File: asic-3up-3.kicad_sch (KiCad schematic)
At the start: 81 parts, among them U24 MCP1824T-1202E/OT, U25 MCP1824T-1202E/OT, U26 MCP1824T-1202E/OT, U27 MCP1824T-0802E, U28 MCP1824T-0802E, U29 MCP1824T-0802E, U30 BM1362AC_MODE1, U31 BM1362AC_MODE0, U32 BM1362AC_MODE1

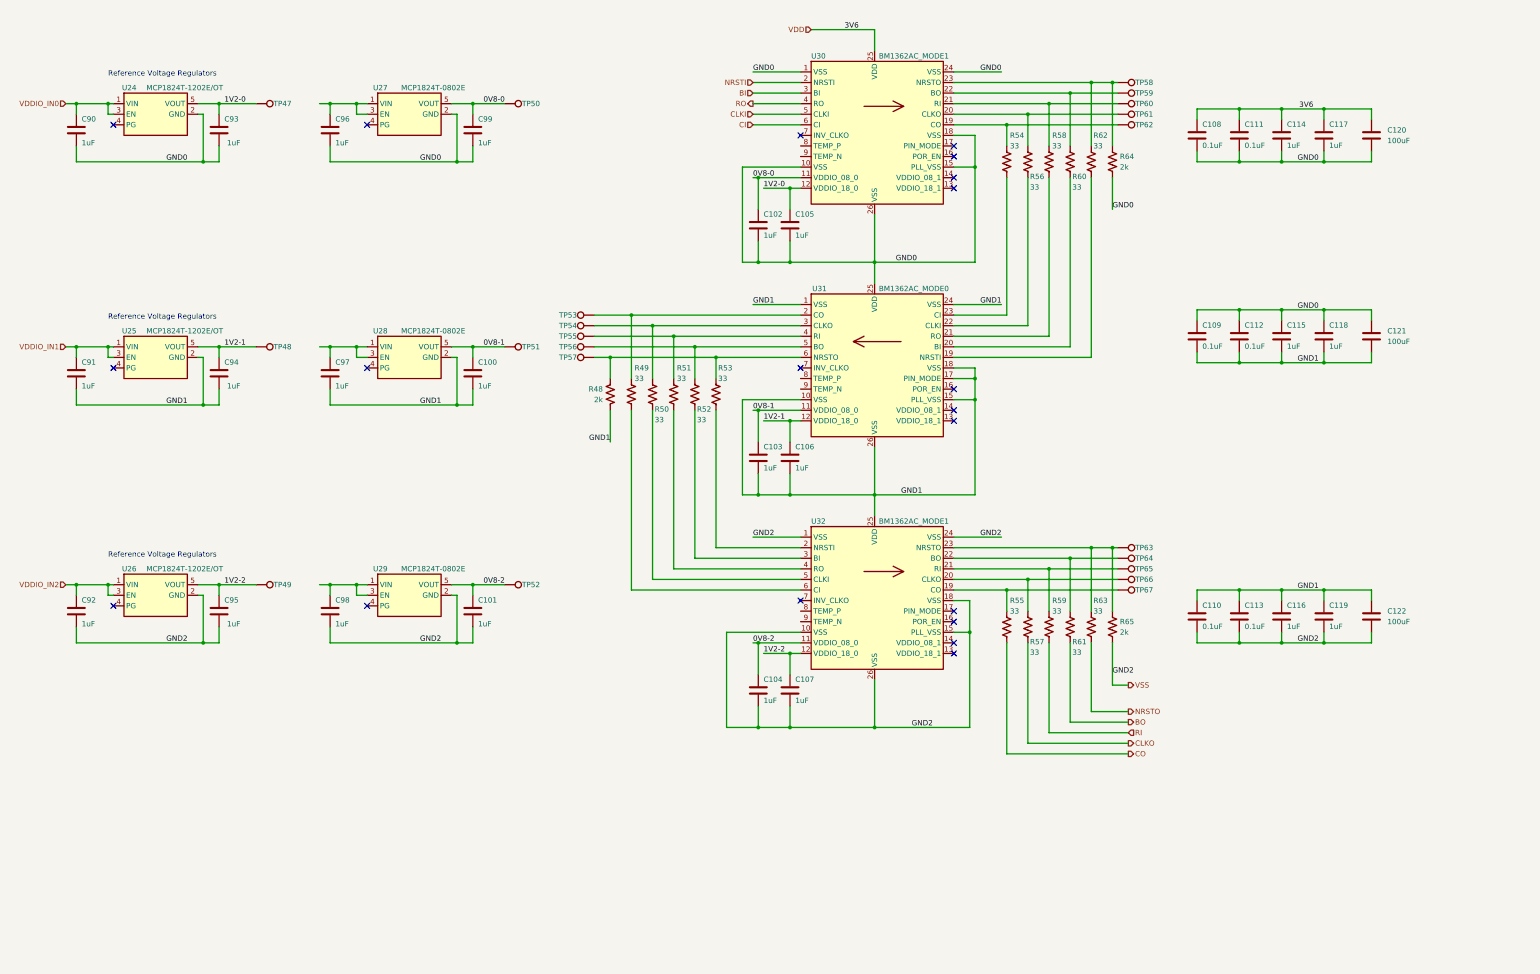
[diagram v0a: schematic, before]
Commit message: added all the ASICs to the schematic. added the RP2040 circuit for data. added the VDDIO boost circuit. schematic cleanup
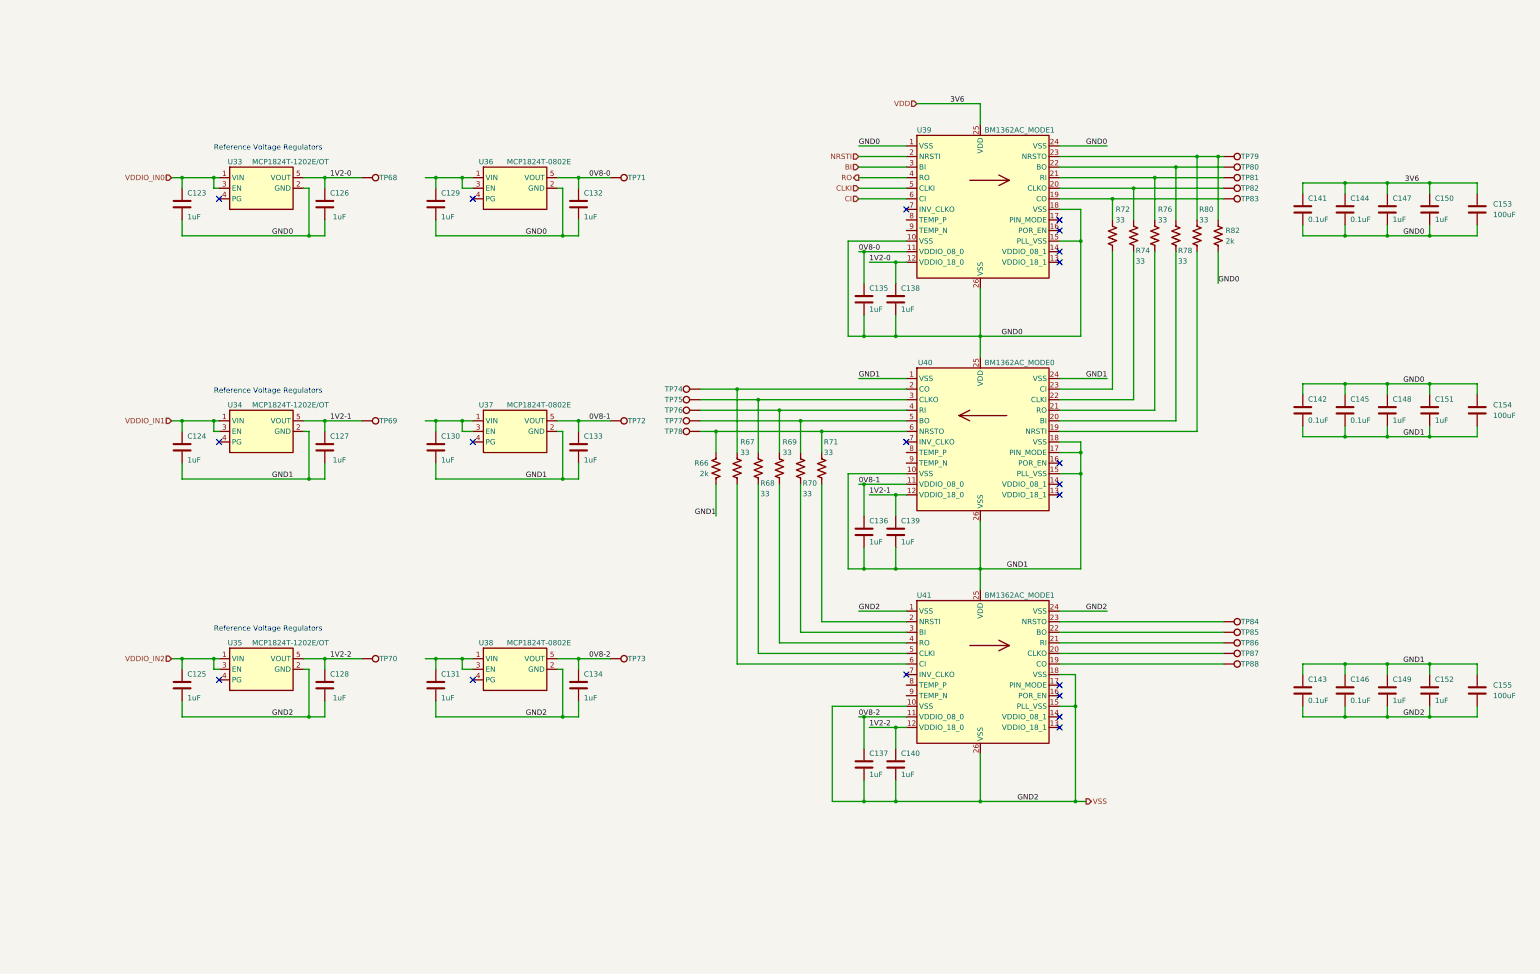
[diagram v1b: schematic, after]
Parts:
- removed R55, R57, R59, R61, R63: 33, Resistor_SMD:R_0402_1005Metric, symbol Device:R_US
- removed R65: 2k, Resistor_SMD:R_0402_1005Metric, symbol Device:R_US
- renumbered C90 to C123, C91 to C124, C92 to C125, C93 to C126, C94 to C127, C95 to C128, C96 to C129, C97 to C130, C98 to C131, C99 to C132, C100 to C133, C101 to C134, C102 to C135, C103 to C136, C104 to C137, C105 to C138, C106 to C139, C107 to C140, C108 to C141, C109 to C142, C110 to C143, C111 to C144, C112 to C145, C113 to C146, C114 to C147, C115 to C148, C116 to C149, C117 to C150, C118 to C151, C119 to C152, C120 to C153, C121 to C154, C122 to C155, R48 to R66, R49 to R67, R50 to R68, R51 to R69, R52 to R70, R53 to R71, R54 to R72, R56 to R74, R58 to R76, R60 to R78, R62 to R80, R64 to R82, TP47 to TP68, TP48 to TP69, TP49 to TP70, TP50 to TP71, TP51 to TP72, TP52 to TP73, TP53 to TP74, TP54 to TP75, TP55 to TP76, TP56 to TP77, TP57 to TP78, TP58 to TP79, TP59 to TP80, TP60 to TP81, TP61 to TP82, TP62 to TP83, TP63 to TP84, TP64 to TP85, TP65 to TP86, TP66 to TP87, TP67 to TP88, U24 to U33, U25 to U34, U26 to U35, U27 to U36, U28 to U37, U29 to U38, U30 to U39, U31 to U40, U32 to U41
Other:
- moved on the sheet: C123, C124, C125, C126, C127, C128, C129, C130, C131, C132, C133, C134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

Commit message: added sweet logo to schematic worksheet. Schematic cleanup.
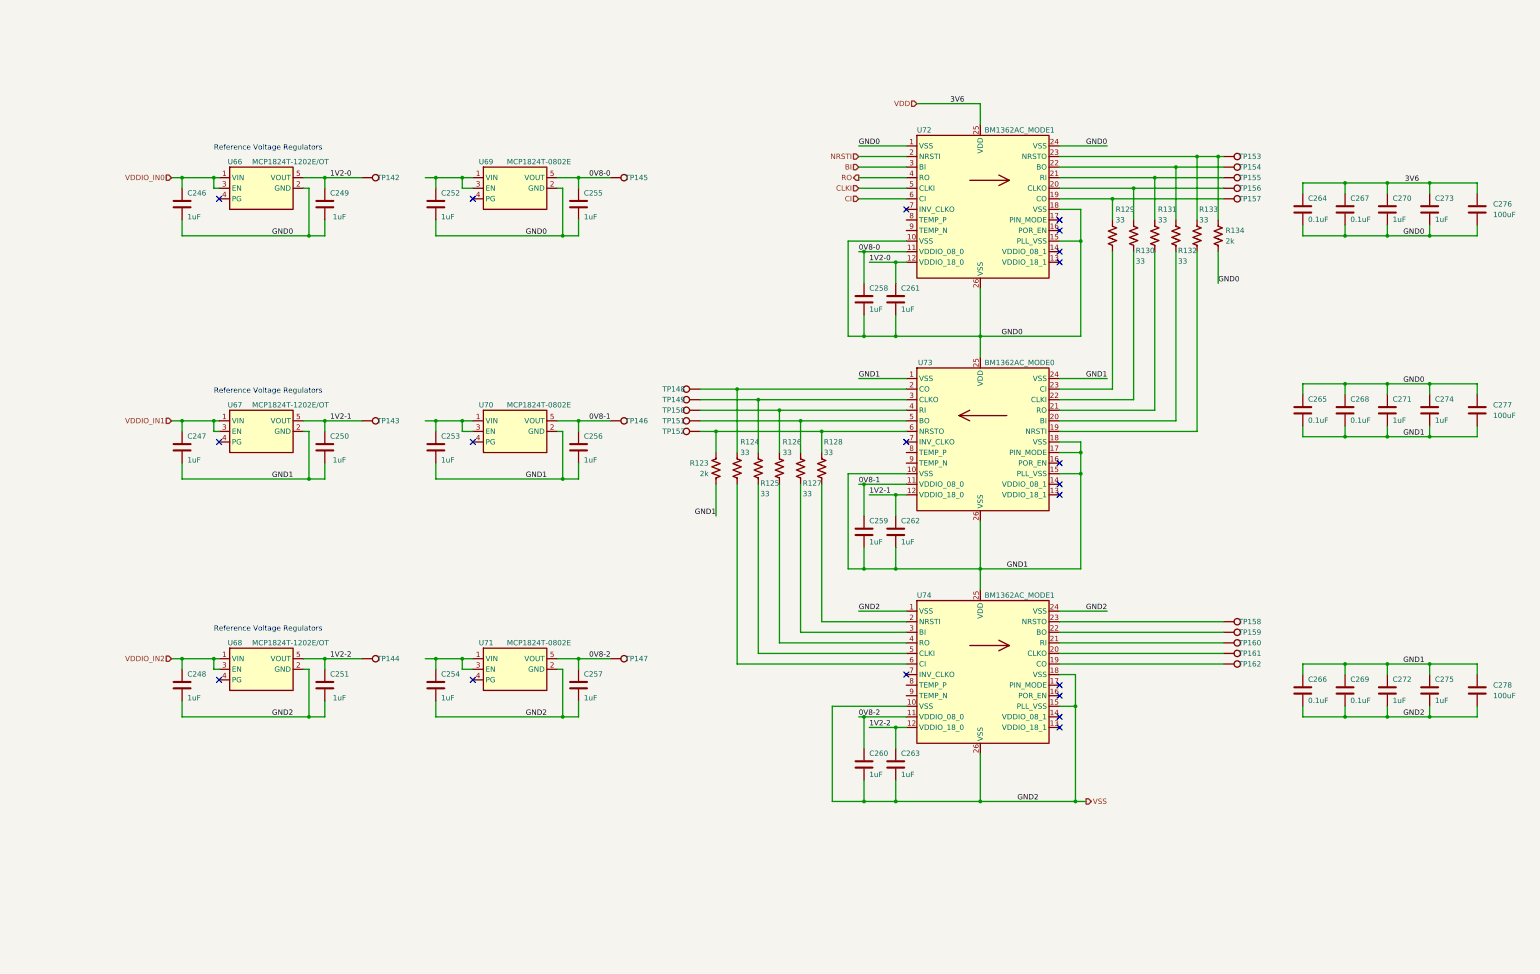
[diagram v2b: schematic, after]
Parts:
- renumbered C123 to C246, C124 to C247, C125 to C248, C126 to C249, C127 to C250, C128 to C251, C129 to C252, C130 to C253, C131 to C254, C132 to C255, C133 to C256, C134 to C257, C135 to C258, C136 to C259, C137 to C260, C138 to C261, C139 to C262, C140 to C263, C141 to C264, C142 to C265, C143 to C266, C144 to C267, C145 to C268, C146 to C269, C147 to C270, C148 to C271, C149 to C272, C150 to C273, C151 to C274, C152 to C275, C153 to C276, C154 to C277, C155 to C278, R66 to R123, R67 to R124, R68 to R125, R69 to R126, R70 to R127, R71 to R128, R72 to R129, R74 to R130, R76 to R131, R78 to R132, R80 to R133, R82 to R134, TP68 to TP142, TP69 to TP143, TP70 to TP144, TP71 to TP145, TP72 to TP146, TP73 to TP147, TP74 to TP148, TP75 to TP149, TP76 to TP150, TP77 to TP151, TP78 to TP152, TP79 to TP153, TP80 to TP154, TP81 to TP155, TP82 to TP156, TP83 to TP157, TP84 to TP158, TP85 to TP159, TP86 to TP160, TP87 to TP161, TP88 to TP162, U33 to U66, U34 to U67, U35 to U68, U36 to U69, U37 to U70, U38 to U71, U39 to U72, U40 to U73, U41 to U74

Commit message: starting layout
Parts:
- added J10, J11: Conn_01x01, emberone:5x9_powertab, symbol Connector_Generic:Conn_01x01
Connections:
- net GND0: now also J10.1 (Pin_1)
- net GND1: now also J11.1 (Pin_1)
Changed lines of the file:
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@@
 	)
 	(junction
+		(at 246.38 99.06)
+		(diameter 0)
+		(color 0 0 0 0)
+	)
+	(junction
 		(at 303.53 62.23)
 		(diameter 0)
@@
 	)
 	(junction
+		(at 246.38 156.21)
+		(diameter 0)
+		(color 0 0 0 0)
+	)
+	(junction
 		(at 226.06 105.41)
 		(diameter 0)
@@
 	(wire
 		(pts
+			(xy 246.38 99.06) (xy 246.38 105.41)
+		)
+		(stroke
+			(width 0)
+			(type default)
+		)
+	)
+	(wire
+		(pts
 			(xy 354.33 194.31) (xy 354.33 196.85)
 		)
@@
 	(wire
 		(pts
-			(xy 246.38 93.98) (xy 246.38 105.41)
+			(xy 246.38 93.98) (xy 246.38 99.06)
 		)
 		(stroke
@@
 	(wire
 		(pts
+			(xy 246.38 156.21) (xy 246.38 161.29)
+		)
+		(stroke
+			(width 0)
+			(type default)
+		)
+	)
+	(wire
+		(pts
 			(xy 334.01 78.74) (xy 334.01 81.28)
 		)
@@
 	(wire
 		(pts
-			(xy 246.38 149.86) (xy 246.38 161.29)
+			(xy 246.38 149.86) (xy 246.38 156.21)
 		)
 		(stroke
@@
 	)
 	(symbol
+		(lib_id "Connector_Generic:Conn_01x01")
+		(at 251.46 156.21 0)
+		(unit 1)
+		(exclude_from_sim no)
+		(in_bom yes)
+		(on_board yes)
+		(dnp no)
+		(property "Reference" "J11"
+			(at 253.746 156.21 0)
+			(effects
+				(font
+					(size 1.27 1.27)
+				)
+				(justify left)
+			)
+		)
+		(property "Value" "Conn_01x01"
+			(at 254 157.4799 0)
+			(effects
+				(font
+					(size 1.27 1.27)
+				)
+				(justify left)
+				(hide yes)
+			)
+		)
+		(property "Footprint" "emberone:5x9_powertab"
+			(at 251.46 156.21 0)
+			(effects
+				(font
+					(size 1.27 1.27)
+				)
+				(hide yes)
+			)
+		)
+		(property "Datasheet" "~"
+			(at 251.46 156.21 0)
+			(effects
+				(font
+					(size 1.27 1.27)
+				)
+				(hide yes)
+			)
+		)
+		(property "Description" "powertab"
+			(at 251.46 156.21 0)
+			(effects
+				(font
+					(size 1.27 1.27)
+				)
+				(hide yes)
+			)
+		)
+		(pin "1"
+		)
+		(instances
+			(project "emberone"
+				(path "/b036224c-4cdf-48cc-81df-19bc5283ebd2/75fd7cab-4b1e-4fa4-8631-02e52962bbf8"
+					(reference "J11")
+					(unit 1)
+				)
+			)
+		)
+	)
+	(symbol
 		(lib_id "Device:C")
 		(at 323.85 190.5 0)
@@
 					(unit 1)
 				)
+			)
+		)
+	)
+	(symbol
+		(lib_id "Connector_Generic:Conn_01x01")
+		(at 251.46 99.06 0)
+		(unit 1)
+		(exclude_from_sim no)
+		(in_bom yes)
+		(on_board yes)
+		(dnp no)
+		(property "Reference" "J10"
+			(at 253.746 99.06 0)
+			(effects
+				(font
+					(size 1.27 1.27)
+				)
+				(justify left)
+			)
+		)
+		(property "Value" "Conn_01x01"
+			(at 254 100.3299 0)
+			(effects
+				(font
+					(size 1.27 1.27)
+				)
+				(justify left)
+				(hide yes)
+			)
+		)
+		(property "Footprint" "emberone:5x9_powertab"
+			(at 251.46 99.06 0)
+			(effects
+				(font
+					(size 1.27 1.27)
+				)
+				(hide yes)
+			)
+		)
+		(property "Datasheet" "~"
+			(at 251.46 99.06 0)
+			(effects
+				(font
+					(size 1.27 1.27)
+				)
+				(hide yes)
+			)
+		)
+		(property "Description" "powertab"
+			(at 251.46 99.06 0)
+			(effects
+				(font
+					(size 1.27 1.27)
+				)
+				(hide yes)
+			)
+		)
+		(pin "1"
+		)
+		(instances
+			(project "emberone"
+				(path "/b036224c-4cdf-48cc-81df-19bc5283ebd2/75fd7cab-4b1e-4fa4-8631-02e52962bbf8"
+					(reference "J10")
+					(unit 1)
+				)
